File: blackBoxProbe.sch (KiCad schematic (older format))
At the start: 77 parts, among them J1 USB-ID, J2 JTAG_2X05, J3 JTAG_2X05, J4 Conn_01x04, Q1 Q_NMOS_DUAL, Q2 Q_PMOS_DUAL, U1 MCP1702-MB, U2 USBLC6-2, U3 STM32F103CBT, U4 74X2T45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

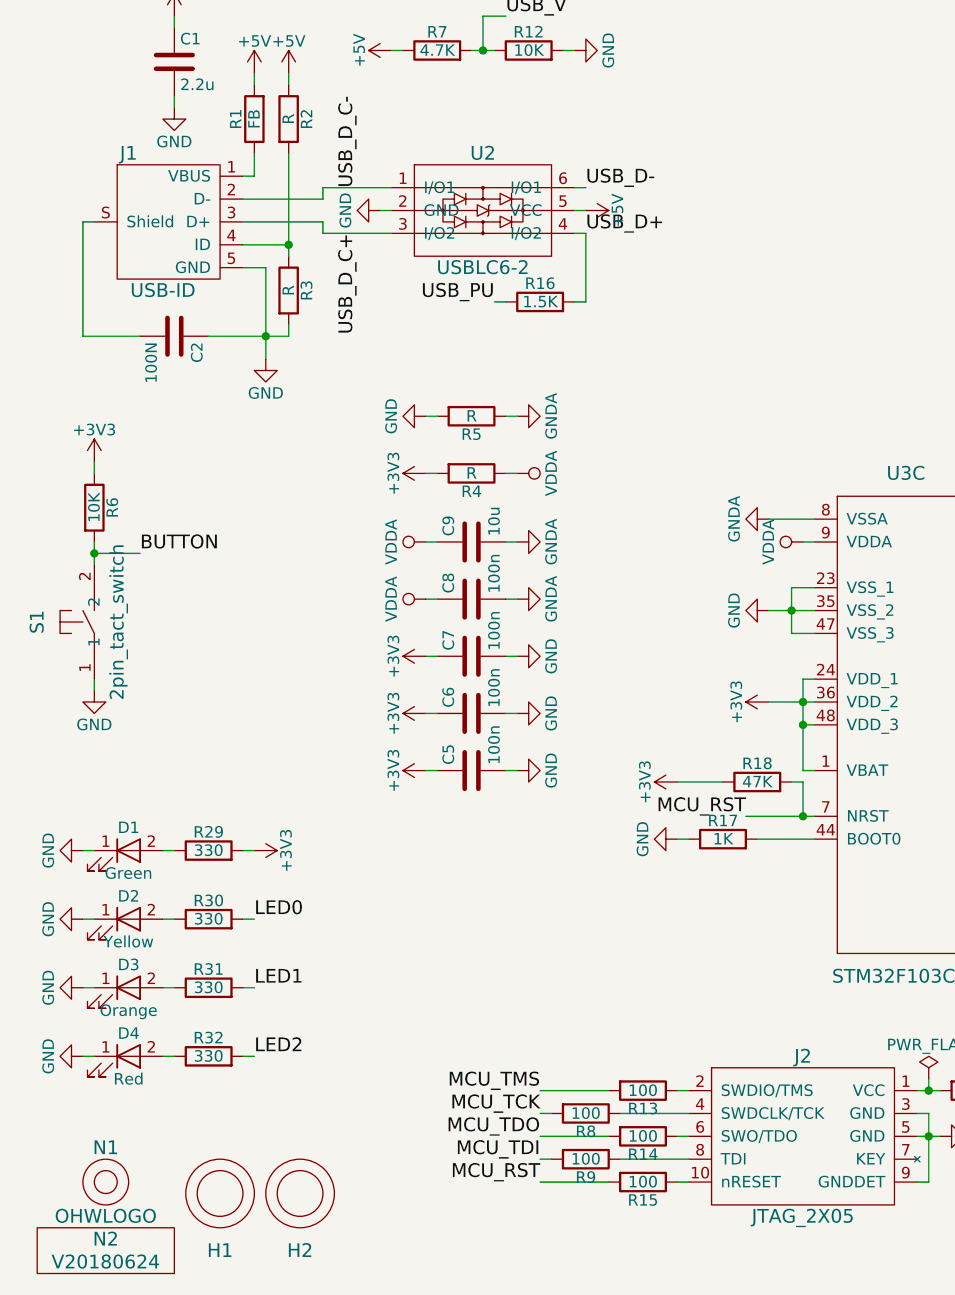
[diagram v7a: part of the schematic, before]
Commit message: FIX: incorrect naming of 74X2T45 gate FIX: missing USB series resistors FIX: added another label for the project name
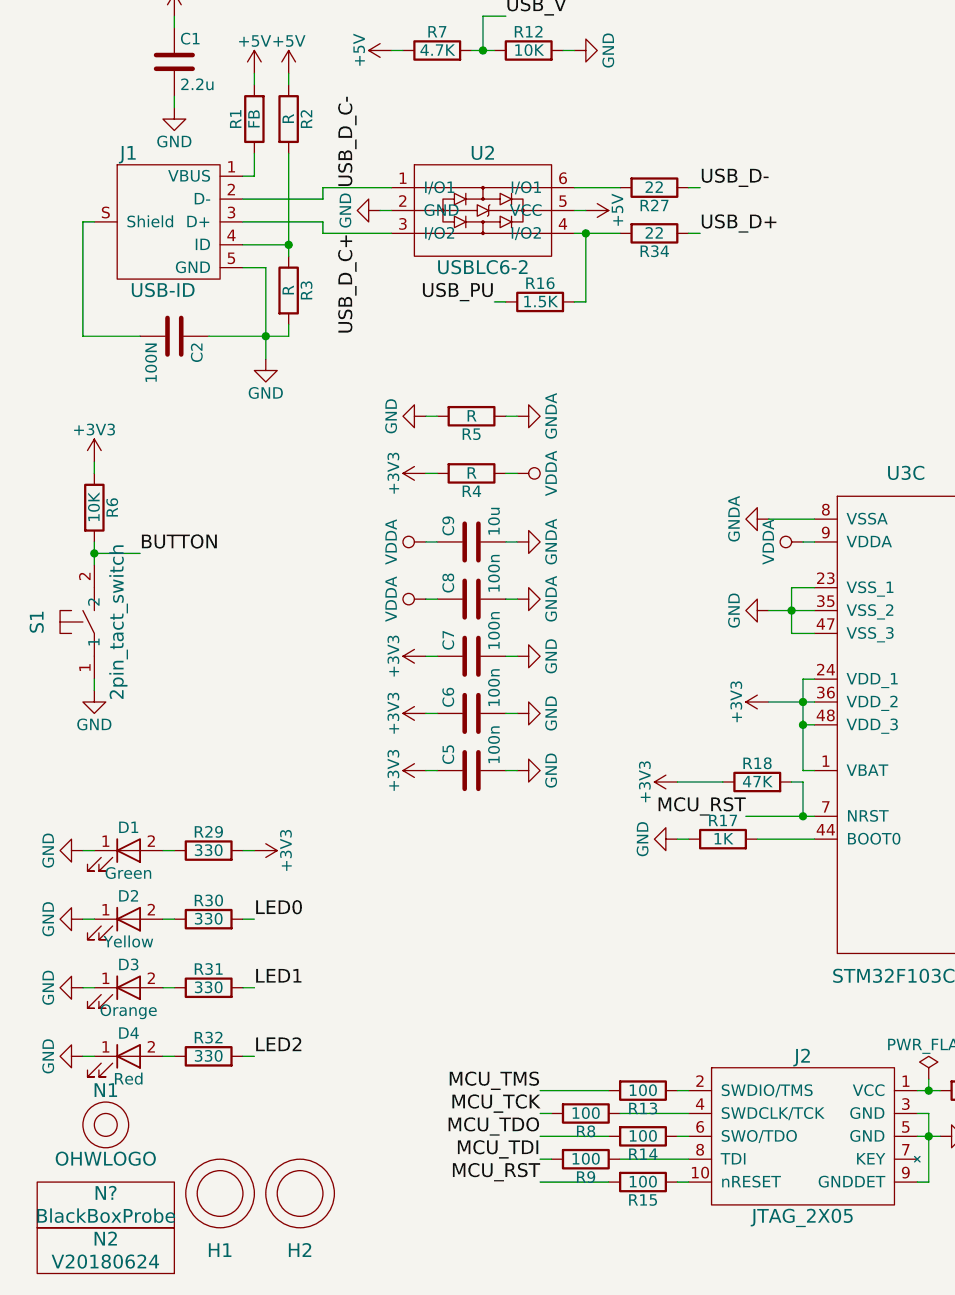
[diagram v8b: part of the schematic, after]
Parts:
- added N?: BlackBoxProbe, SquantorLabels:Label_version, symbol VYYYYMMDD
- added R27, R34: 22, SquantorRcl:R_0603_hand, symbol R
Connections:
- net USB_D+: now also R34.1; no longer R16.2, U2.4 (I/O2)
- net USB_D-: now also R27.1; no longer U2.6 (I/O1)
- new net: R16.2, R34.2, U2.4 (I/O2)
- new net: R27.2, U2.6 (I/O1)
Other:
- moved on the sheet: N1
